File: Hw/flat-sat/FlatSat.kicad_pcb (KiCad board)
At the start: 4 copper layers, 48 x 32 mm, 90 parts, among them J1 Antenna, J2 Antenna, J3 periphs, J4 SWD, P1 USB_C_Plug_USB2.0, U1 TLV75733PDBVR, U10 LIS2DH, U11 BME280 /BMP280, U2 0900FM15D0039, U3 PE42421, U4 SX1262IMLTRT, U5 W25Q16JV, U6 0900FM15D0039, U7 PE42421, U8 SX1262IMLTRT, U9 RP2040, Y1 32Mhz, Y2 32Mhz, Y3 12MHz

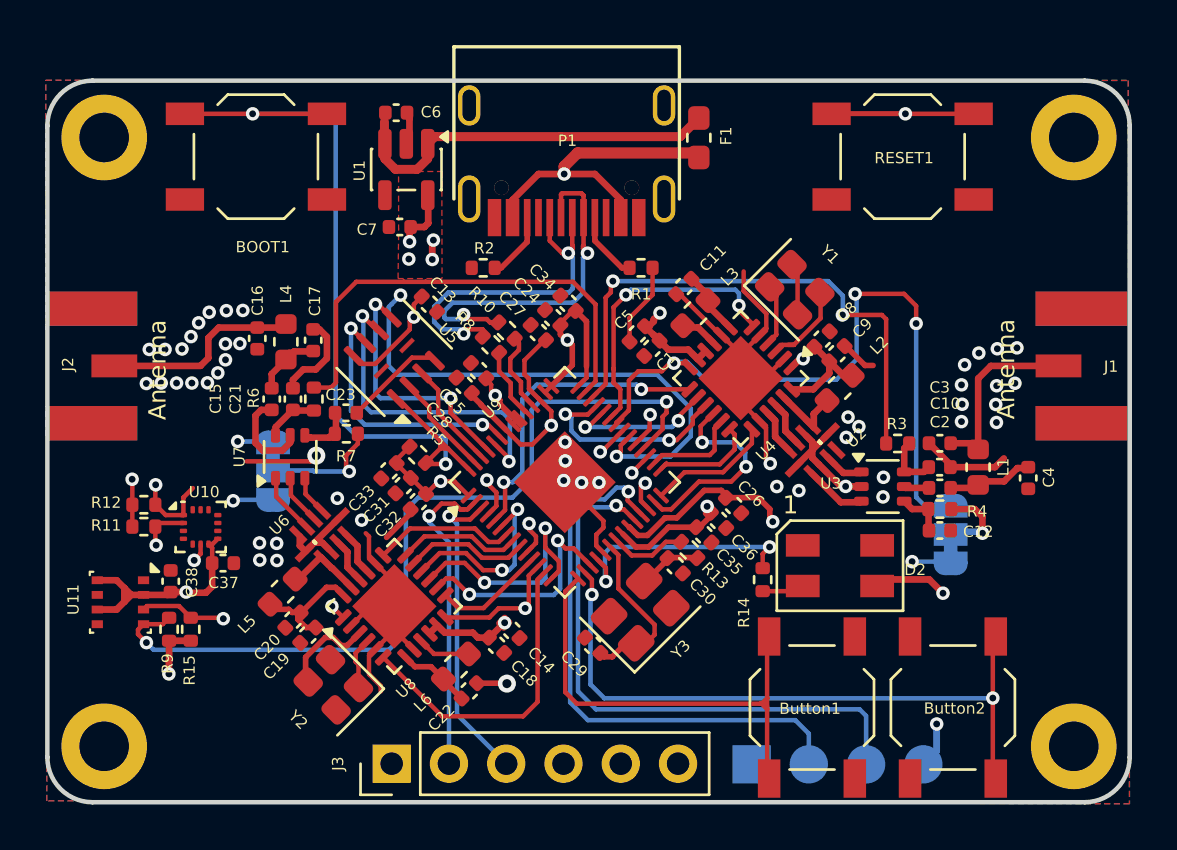
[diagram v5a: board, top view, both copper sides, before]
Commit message: feat(Hw):Update_PCB_Change_Buttons
Pending_Check_LIS2DH
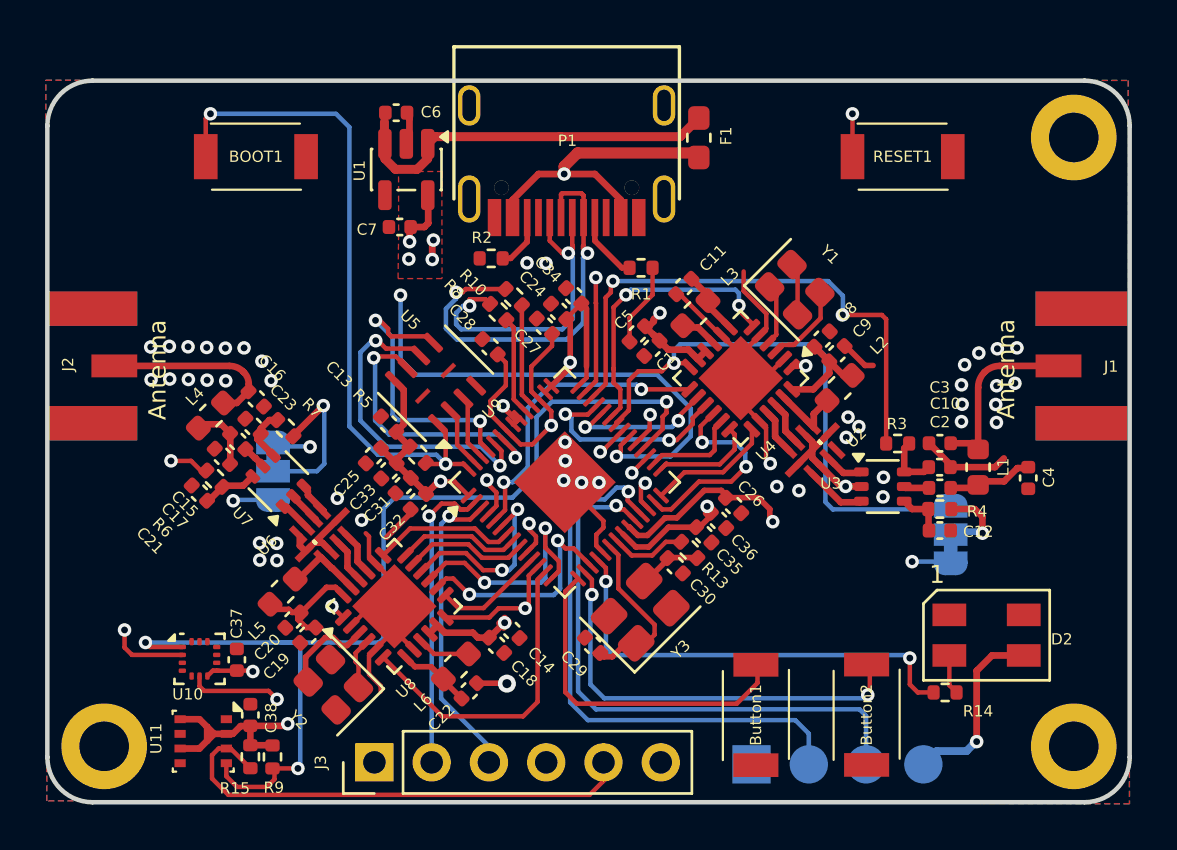
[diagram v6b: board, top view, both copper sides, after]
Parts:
- removed ?: , 
- removed R11, R12: 10k, Resistor_SMD:R_0402_1005Metric
- BOOT1, Button1, Button2, RESET1: footprint Button_Switch_SMD:SW_SPST_TL3342 -> FlatSat:TS1088R02026
- moved R14 9.51 mm to (118.5, 122.1), turned to 180 degrees
- moved R9 7.28 mm to (88.7, 125.0), turned to -90 degrees
- moved D2 7.20 mm to (120.4, 119.6)
- moved U11 7.18 mm to (85.6, 124.3)
- moved C38 6.90 mm to (87.7, 123.1)
- moved C17 6.54 mm to (86.5, 111.7), turned to 135 degrees
- moved R15 6.24 mm to (87.7, 125.0), turned to -90 degrees
- moved C25 5.99 mm to (93.2, 111.6), turned to -135 degrees
- moved C21 5.88 mm to (85.5, 113.3), turned to 135 degrees
- moved U10 5.85 mm to (85.5, 120.6)
- moved R6 5.65 mm to (86.1, 112.7), turned to 135 degrees
- moved C13 5.62 mm to (93.9, 110.2), turned to 135 degrees
- moved L4 4.67 mm to (86.0, 109.8), turned to -135 degrees
- moved C37 4.33 mm to (87.1, 120.7), turned to 90 degrees
- moved C23 4.16 mm to (87.8, 110.3), turned to 135 degrees
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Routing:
- net /SDA: track 54.1 -> 71.6 mm, vias 3 -> 2
- net GND: track 74.7 -> 62.2 mm, vias 50 -> 47
- net /R1_ANT_SW: track 21.0 -> 32.8 mm, vias 0 -> 2
- net /Butt_2: track 29.7 -> 19.2 mm
- net /RESET: track 38.3 -> 28.3 mm
- net /LED1: track 10.9 -> 20.1 mm
- net /Butt_1: track 21.6 -> 15.2 mm
- net /QSPI_SS: track 36.9 -> 30.5 mm
- net /R0_DIO2: track 30.0 -> 25.1 mm, vias 3 -> 1
- net +3V3: track 64.9 -> 61.5 mm, vias 20 -> 17
- net Net-(U7-RFC): track 4.19 -> 1.10 mm
- net /INT1: track 46.6 -> 49.6 mm
- net /DIO23: track 24.4 -> 21.4 mm
- net /D-: track 16.0 -> 18.6 mm
- net +1V2: track 31.5 -> 33.4 mm
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
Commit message: feat(Hw):Logos_Added
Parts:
- added G***: LOGO, Aesthetics:electronic_cats_logo_4x3, B.Cu at (120.1, 100.8)
- added REF**: OSHW-Logo_5.7x6mm_SilkScreen, Symbol:OSHW-Logo_5.7x6mm_SilkScreen, B.Cu at (86.7, 121.7)
- added kibuzzard-69651236: G***, kibuzzard-69651236, F.Cu at (88.0, 100.8)
- added kibuzzard-69651254: G***, kibuzzard-69651254, F.Cu at (116.8, 100.7)
- added kibuzzard-696512BA: G***, kibuzzard-696512BA, B.Cu at (109.8, 122.4)
- added kibuzzard-696512BA: G***, kibuzzard-696512BA, B.Cu at (93.2, 122.4)
- added kibuzzard-696512FB: G***, kibuzzard-696512FB, B.Cu at (100.8, 122.4)
- added kibuzzard-69651304: G***, kibuzzard-69651304, B.Cu at (103.5, 122.4)
- added kibuzzard-6965130C: G***, kibuzzard-6965130C, B.Cu at (106.0, 122.4)
- added kibuzzard-69651319: G***, kibuzzard-69651319, B.Cu at (95.7, 122.4)
- added kibuzzard-69651321: G***, kibuzzard-69651321, B.Cu at (98.2, 122.4)
- added kibuzzard-6965136B: G***, kibuzzard-6965136B, B.Cu at (117.6, 122.4)
- added kibuzzard-69651375: G***, kibuzzard-69651375, B.Cu at (115.0, 122.4)
- added kibuzzard-69651380: G***, kibuzzard-69651380, B.Cu at (112.5, 122.4)
- added kibuzzard-69651BF8: G***, kibuzzard-69651BF8, B.Cu at (102.6, 109.6)
- added kibuzzard-69652909: G***, kibuzzard-69652909, F.Cu at (110.2, 118.6)
- added kibuzzard-69652922: G***, kibuzzard-69652922, F.Cu at (115.0, 118.6)
- added kibuzzard-69652959: G***, kibuzzard-69652959, F.Cu at (86.8, 102.9)

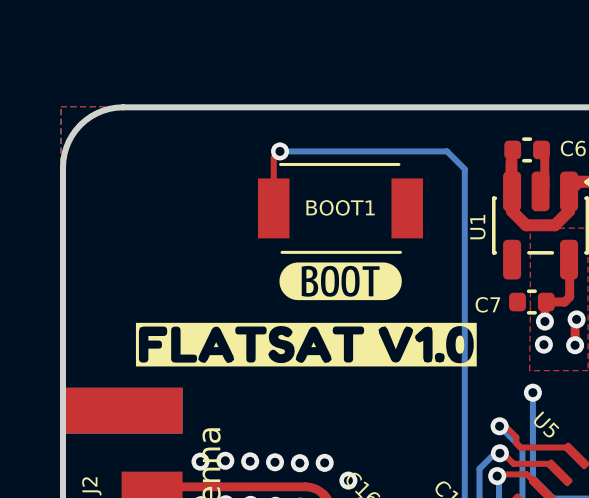
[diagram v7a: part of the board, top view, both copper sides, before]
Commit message: feate(Hw):Updated_logos
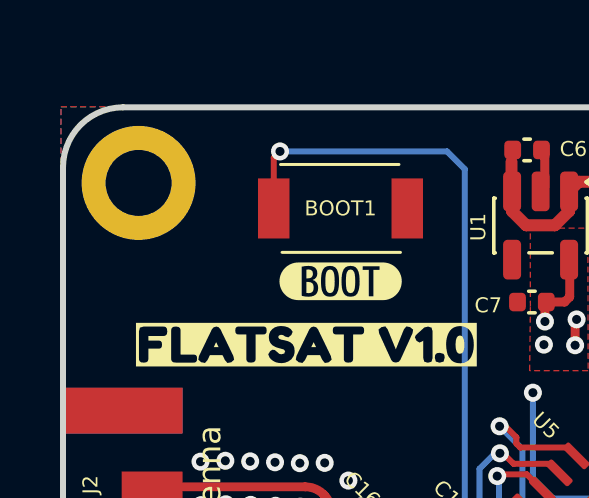
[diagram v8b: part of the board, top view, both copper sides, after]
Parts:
- removed the G*** at (120.1, 100.8)
- removed kibuzzard-69651BF8: G***, kibuzzard-69651BF8
- added ?: , , F.Cu at (81.4, 97.5)
- added G***: LOGO, Aesthetics:electronic_cats_logo_8x6, B.Cu at (112.5, 101.0)
- added kibuzzard-69653048: G***, kibuzzard-69653048, B.Cu at (102.0, 111.6)
